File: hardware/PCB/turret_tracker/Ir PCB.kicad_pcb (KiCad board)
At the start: 2 copper layers, 60 x 60 mm, 15 parts, among them J1 Payload_tracker_connector, M2 FinMount

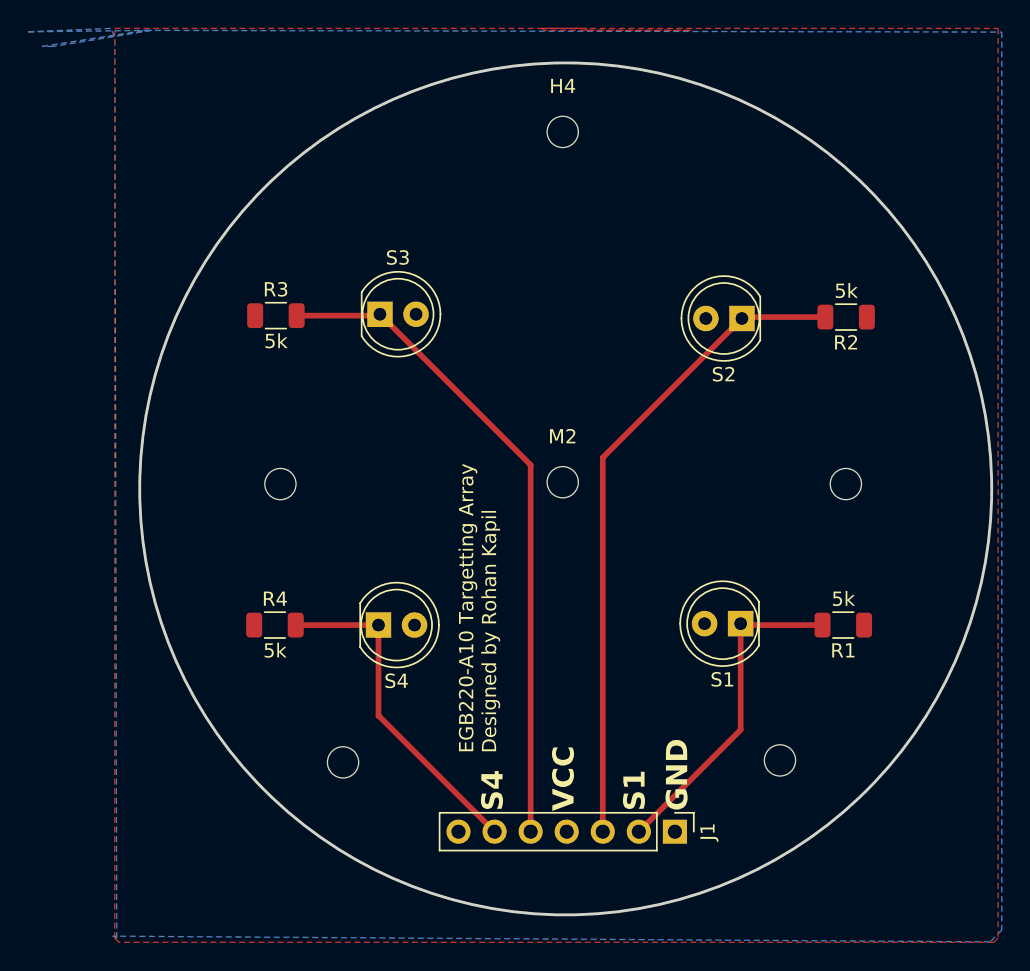
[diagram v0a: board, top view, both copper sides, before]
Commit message: Code clean up, debug state added, state machine for payload added
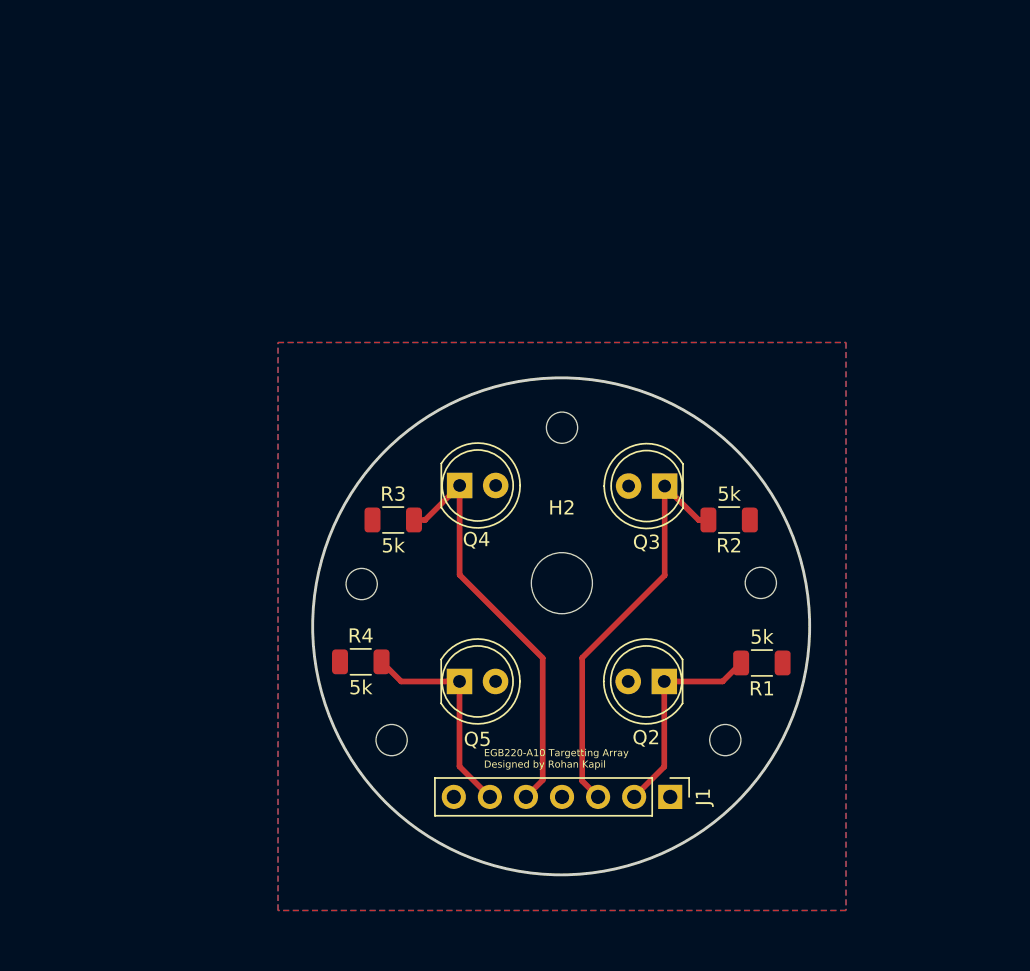
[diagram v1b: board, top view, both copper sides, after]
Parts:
- removed M2: FinMount, MountingHole:MountingHole_2.2mm_M2
- added H2: FinMount, MountingHole:MountingHole_4.3mm_M4, F.Cu at (150.0, 107.0)
- Q5: renamed from SFH309; value S4 -> SFH309
- moved H4 20.8 mm to (150.0, 96.0)
- moved R3 16.6 mm to (138.1, 102.5)
- moved R2 16.5 mm to (161.8, 102.5)
- moved Q4 13.3 mm to (142.8, 100.1)
- moved Q3 13.0 mm to (157.2, 100.1)
- moved H7 9.18 mm to (164.0, 106.9)
- moved H6 9.07 mm to (135.9, 107.0)
- moved Q5 6.95 mm to (142.8, 113.9)
- moved Q2 6.75 mm to (157.2, 113.9)
- moved R4 6.58 mm to (135.8, 112.5)
- moved R1 6.32 mm to (164.1, 112.6)
- moved H8 4.11 mm to (161.5, 118.0)
- moved H5 3.76 mm to (138.0, 118.0)
- moved J1 2.47 mm to (157.6, 122.0)
- renumbered S1 to Q2, S2 to Q3, S3 to Q4
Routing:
- net /S2: track 46.2 -> 28.6 mm
- net /S3: track 46.7 -> 29.3 mm
- net /S4: track 23.8 -> 14.9 mm
- net /S1: track 23.4 -> 15.2 mm
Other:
- board size 60 x 60 mm -> 35 x 35 mm
- board text removed: "GND"
- board text removed: "S1"
- board text removed: "S4"
- board text removed: "VCC"
